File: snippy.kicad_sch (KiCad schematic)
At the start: 9 parts, among them J1 USB_A, SW1 SW_Push, SW2 SW_Push, SW3 SW_Push, SW4 SW_Push, U1 CH552G

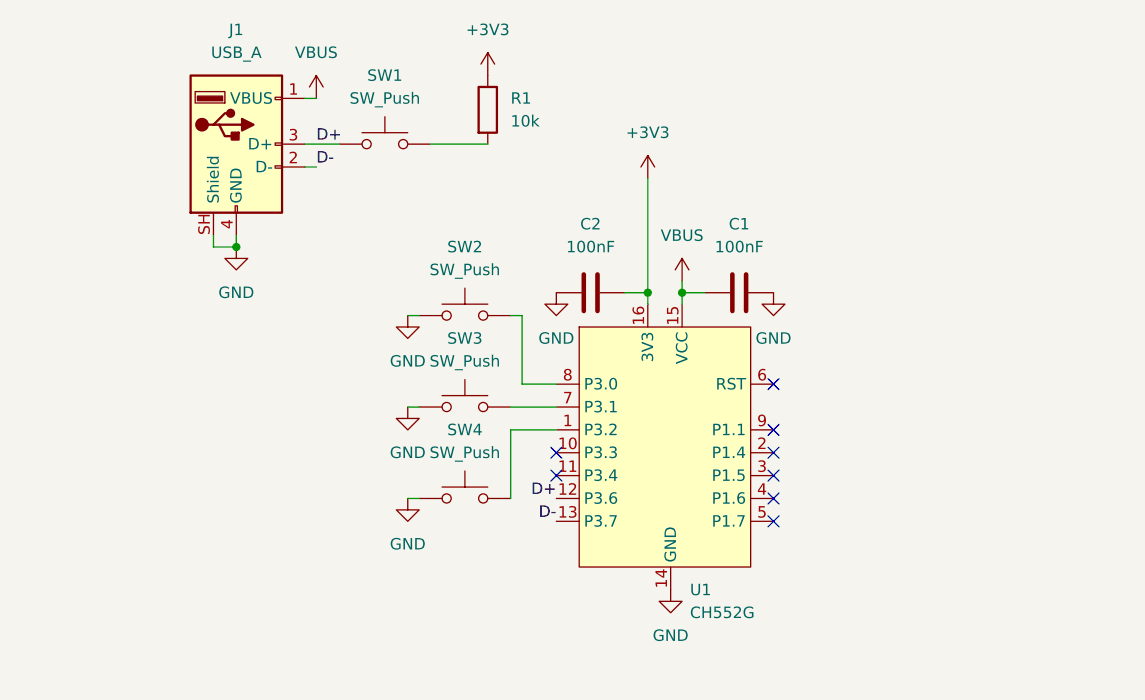
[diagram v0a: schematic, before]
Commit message: add leds
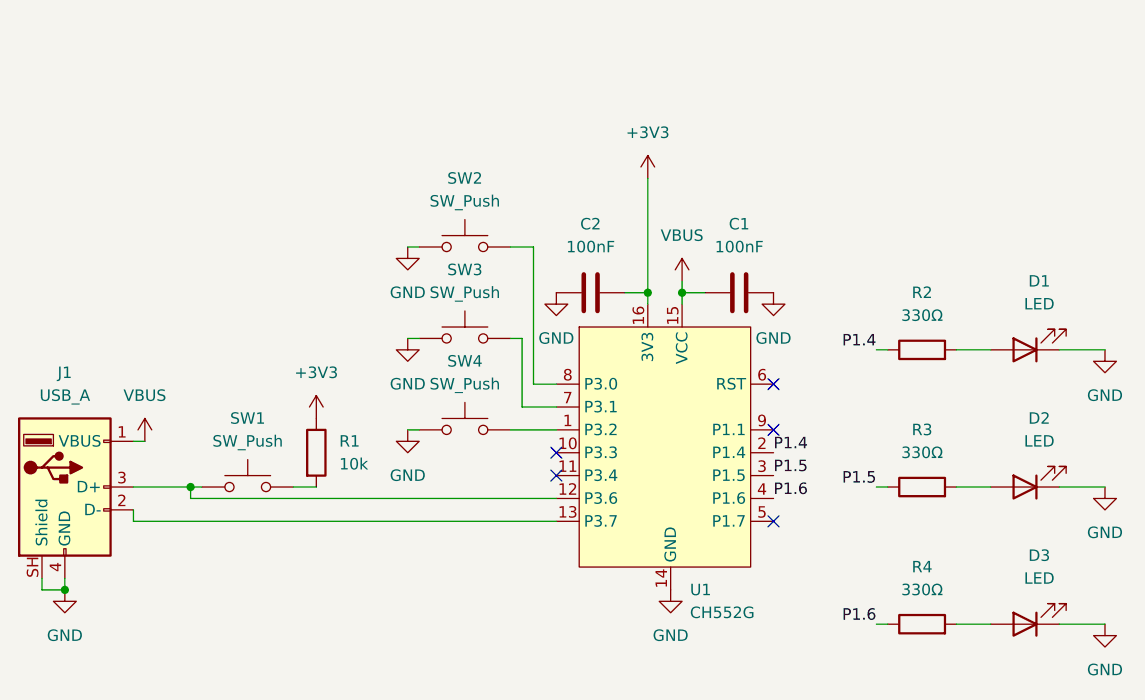
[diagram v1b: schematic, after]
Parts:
- added D1, D2, D3: LED, LED_SMD:LED_0805_2012Metric, symbol Device:LED
- added R2, R3, R4: 330Ω, Resistor_SMD:R_0603_1608Metric, symbol Device:R
- SW2, SW3, SW4: footprint Button_Switch_SMD:SW_SPST_TS-1088-xR020 -> Button_Switch_THT:SW_PUSH_6mm
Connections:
- net GND: now also D1.1 (K), D2.1 (K), D3.1 (K)
- net P1.4: now reaches U1.2 (P1.4)
- net P1.4: now also R2.1
- net P1.5: now reaches U1.3 (P1.5)
- net P1.5: now also R3.1
- net P1.6: now reaches U1.4 (P1.6)
- net P1.6: now also R4.1
- net D-: no longer names the net of J1.2 (D-), U1.13 (P3.7)
- new net: D3.2 (A), R4.2
- new net: D1.2 (A), R2.2
- new net: D2.2 (A), R3.2
- no-connect marks 8 -> 5
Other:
- moved on the sheet: J1, R1, SW1, SW2, SW3, SW4

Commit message: finish routing!
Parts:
- removed D1, D2, D3: LED, LED_SMD:LED_0805_2012Metric, symbol Device:LED
- removed R2, R3, R4: 330Ω, Resistor_SMD:R_0603_1608Metric, symbol Device:R
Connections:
- net D+: now reaches J1.3 (D+), SW1.1, U1.12 (P3.6)
- net D-: now reaches J1.2 (D-), U1.13 (P3.7)
- net P1.4: no longer names the net of U1.2 (P1.4)
- net P1.5: no longer names the net of U1.3 (P1.5)
- net P1.6: no longer names the net of U1.4 (P1.6)
- no-connect marks 5 -> 8
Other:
- moved on the sheet: J1, R1, SW1
